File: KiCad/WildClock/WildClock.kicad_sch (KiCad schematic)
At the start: 33 parts, among them J1 UART, Q1 CA1, Q2 CA2, Q3 CA3, Q4 CA4, SW1 ButtonUp, SW2 ButtonDown, SW3 ButtonOK, U1 ESP32-C3-MINI-1, U3 74HC595, U4 TiltSensor

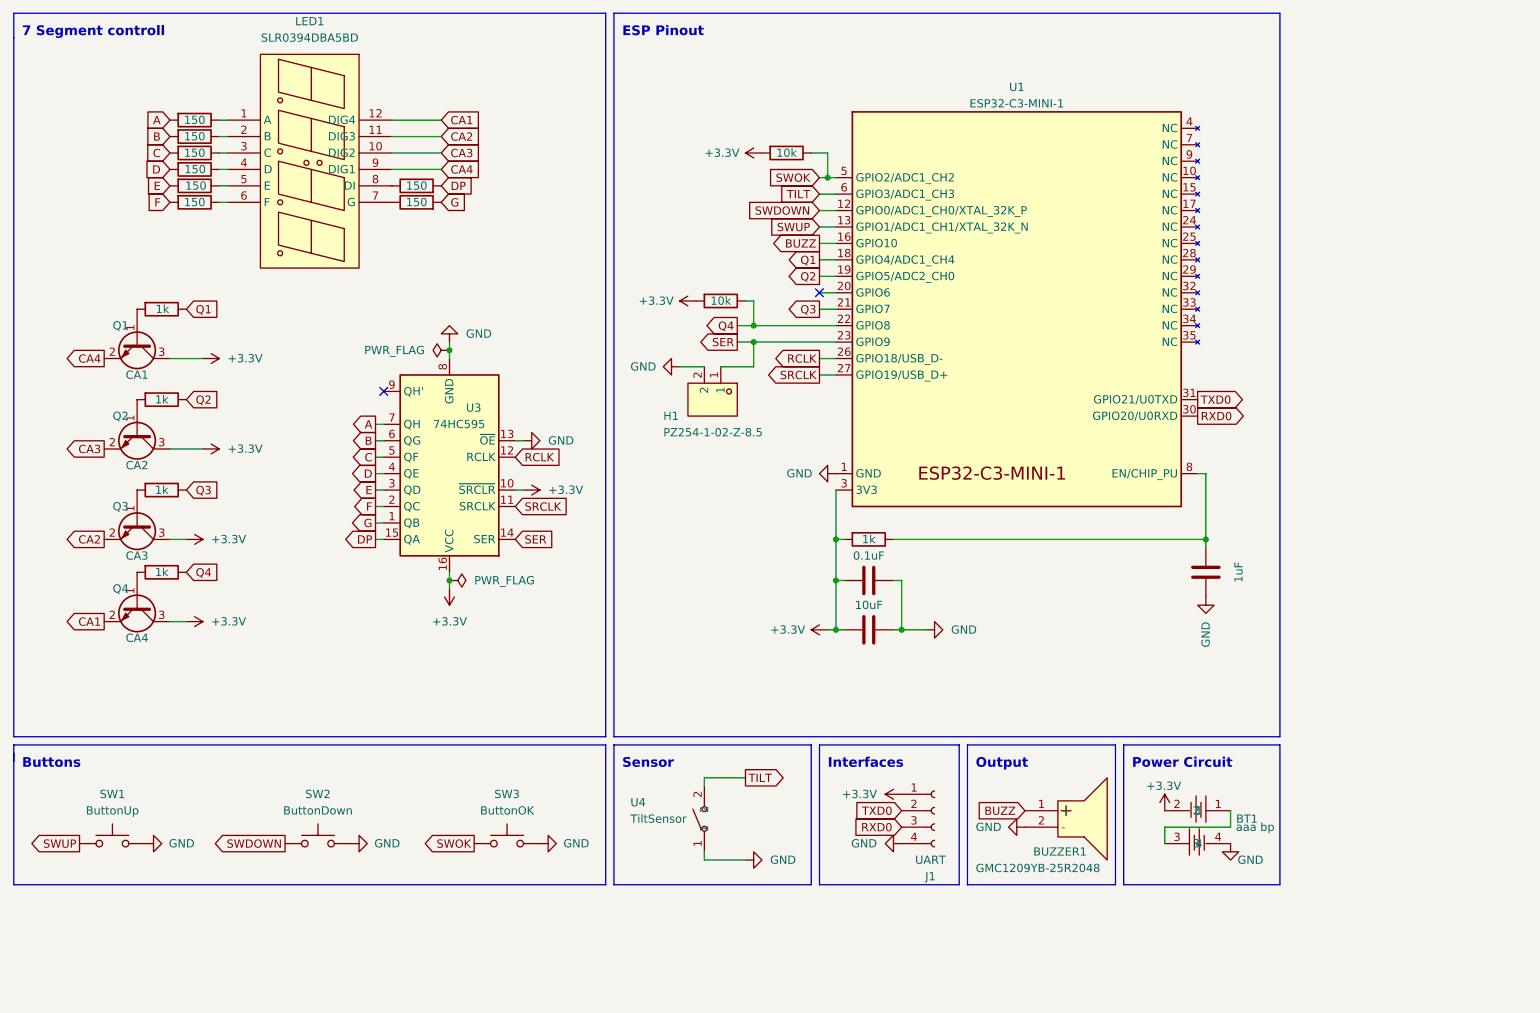
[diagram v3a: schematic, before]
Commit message: use lcsc footprints
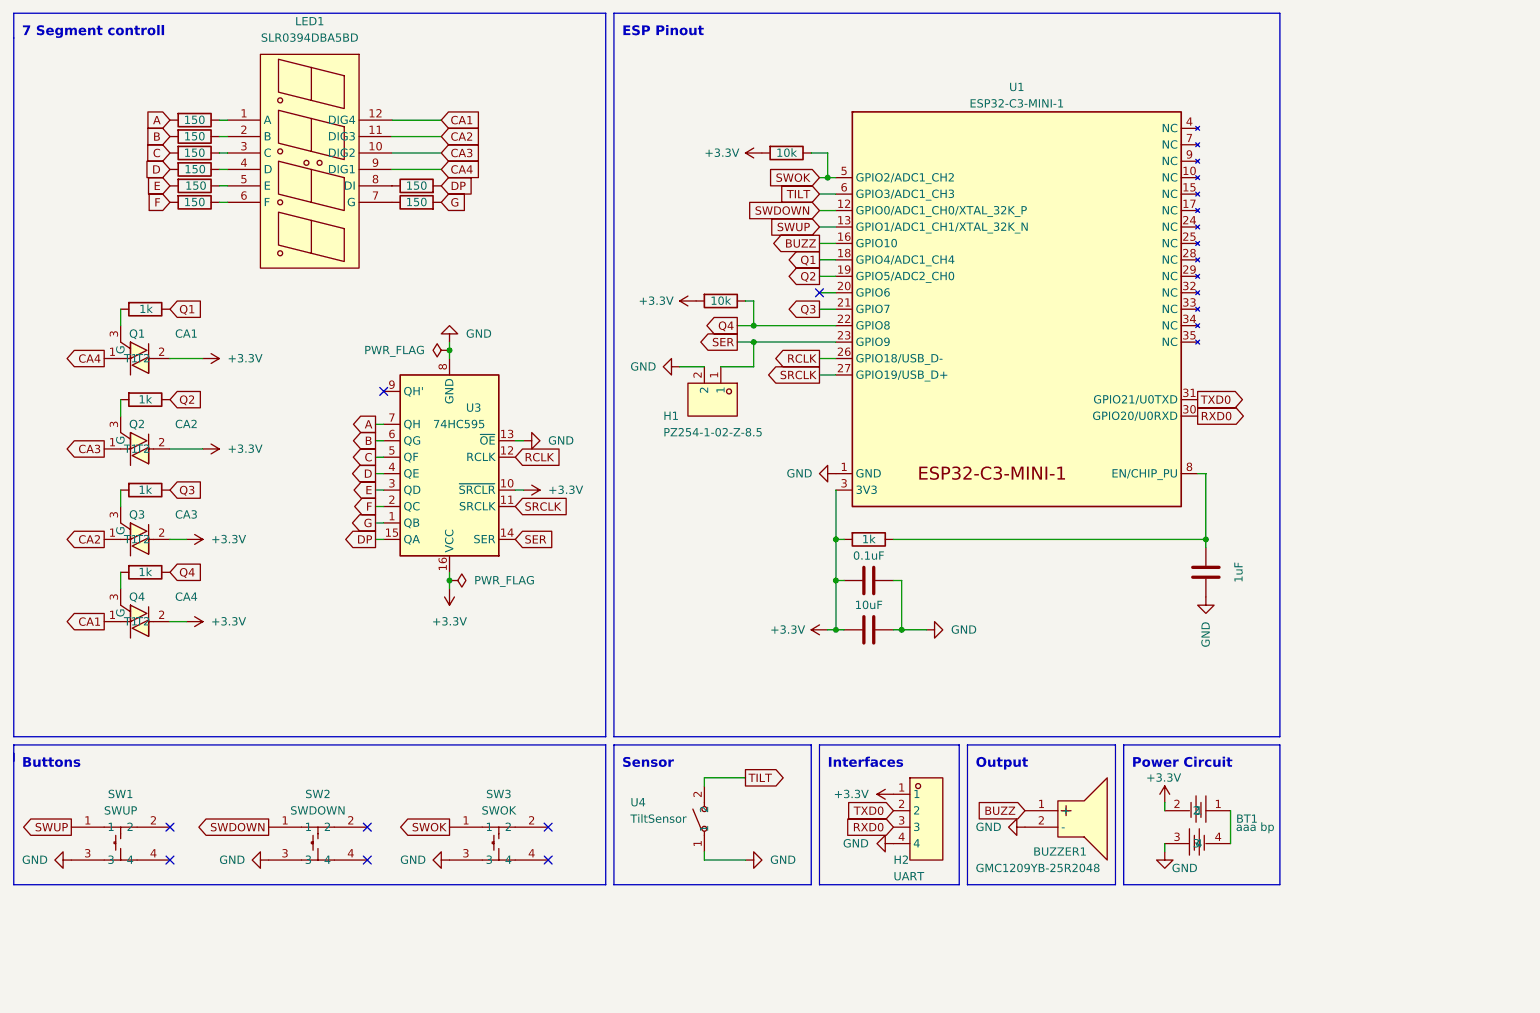
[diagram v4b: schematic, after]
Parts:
- removed J1: UART, Connector_PinHeader_1.00mm:PinHeader_1x04_P1.00mm_Vertical, symbol Connector:Conn_01x04_Female
- removed Q1: CA1, Package_TO_SOT_SMD:SOT-23, symbol Transistor_BJT:MMBT3904
- removed Q2: CA2, Package_TO_SOT_SMD:SOT-23, symbol Transistor_BJT:MMBT3904
- removed Q3: CA3, Package_TO_SOT_SMD:SOT-23, symbol Transistor_BJT:MMBT3904
- removed Q4: CA4, Package_TO_SOT_SMD:SOT-23, symbol Transistor_BJT:MMBT3904
- removed SW1: ButtonUp, Button_Switch_SMD:SW_Push_1P1T_NO_6x6mm_H9.5mm, symbol Switch:SW_Push
- removed SW2: ButtonDown, Button_Switch_SMD:SW_Push_1P1T_NO_6x6mm_H9.5mm, symbol Switch:SW_Push
- removed SW3: ButtonOK, Button_Switch_SMD:SW_Push_1P1T_NO_6x6mm_H9.5mm, symbol Switch:SW_Push
- added H2: UART, easyeda2kicad:HDR-TH_4P-P2.54-V-M, symbol easyeda2kicad:PZ254-1-04-Z-8.5
- added Q1: CA1, easyeda2kicad:SOT-23-3_L2.9-W1.3-P1.90-LS2.4-BR-CW, symbol easyeda2kicad:BT169-23
- added Q2: CA2, easyeda2kicad:SOT-23-3_L2.9-W1.3-P1.90-LS2.4-BR-CW, symbol easyeda2kicad:BT169-23
- added Q3: CA3, easyeda2kicad:SOT-23-3_L2.9-W1.3-P1.90-LS2.4-BR-CW, symbol easyeda2kicad:BT169-23
- added Q4: CA4, easyeda2kicad:SOT-23-3_L2.9-W1.3-P1.90-LS2.4-BR-CW, symbol easyeda2kicad:BT169-23
- added SW1: SWUP, easyeda2kicad:SW-TH_4P-L6.0-W6.0-P4.50-LS6.5, symbol easyeda2kicad:TS-1002-10526
- added SW2: SWDOWN, easyeda2kicad:SW-TH_4P-L6.0-W6.0-P4.50-LS6.5, symbol easyeda2kicad:TS-1002-10526
- added SW3: SWOK, easyeda2kicad:SW-TH_4P-L6.0-W6.0-P4.50-LS6.5, symbol easyeda2kicad:TS-1002-10526
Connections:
- net +3.3V: now also H2.1, Q1.2 (T2), Q2.2 (T2), Q3.2 (T2), Q4.2 (T2)
- net CA1: now also Q4.1 (T1)
- net CA2: now also Q3.1 (T1)
- net CA3: now also Q2.1 (T1)
- net CA4: now also Q1.1 (T1)
- net GND: now also BT1.3, H2.4, SW1.3, SW2.3, SW3.3; no longer BT1.4
- net RXD0: now also H2.3
- net SWDOWN: now also SW2.1
- net SWOK: now also SW3.1
- net SWUP: now also SW1.1
- net TXD0: now also H2.2
- net at R2.2: now also Q2.3 (G)
- net at R4.2: now also Q4.3 (G)
- net at R1.2: now also Q1.3 (G)
- net at BT1.1: now also BT1.4; no longer BT1.3
- net at R3.2: now also Q3.3 (G)
- no-connect marks 2 -> 8

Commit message: implemented maxis changes
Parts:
- removed Q1: CA1, easyeda2kicad:SOT-23-3_L2.9-W1.3-P1.90-LS2.4-BR-CW, symbol easyeda2kicad:BT169-23
- removed Q2: CA2, easyeda2kicad:SOT-23-3_L2.9-W1.3-P1.90-LS2.4-BR-CW, symbol easyeda2kicad:BT169-23
- removed Q3: CA3, easyeda2kicad:SOT-23-3_L2.9-W1.3-P1.90-LS2.4-BR-CW, symbol easyeda2kicad:BT169-23
- removed Q4: CA4, easyeda2kicad:SOT-23-3_L2.9-W1.3-P1.90-LS2.4-BR-CW, symbol easyeda2kicad:BT169-23
- added Q1, Q2, Q3, Q4: AO3401A, Package_TO_SOT_SMD:SOT-23, symbol Transistor_FET:AO3401A
- added Q5: AO3400A, Package_TO_SOT_SMD:SOT-23, symbol Transistor_FET:AO3400A
- added R5: 1k, Resistor_SMD:R_0805_2012Metric, symbol Device:R
- R2: value 1k -> 70
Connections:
- net +3.3V: now also R2.1, Q1.2 (S), Q2.2 (S), Q3.2 (S), Q4.2 (S)
- net BUZZ: now also Q5.1 (G); no longer BUZZER1.1 (+)
- net CA1: now also Q4.3 (D)
- net CA2: now also Q3.3 (D)
- net CA3: now also Q2.3 (D)
- net CA4: now also Q1.3 (D)
- net GND: now also Q5.2 (S); no longer BUZZER1.2 (-)
- net Q1: now also R1.2; no longer R1.1
- net Q2: now also R3.2; no longer R2.1
- net Q3: now also R4.2; no longer R3.1
- net Q4: now also R5.2; no longer R4.1
- net at R2.2: now also BUZZER1.1 (+)
- new net: Q2.1 (G), R3.1
- new net: Q1.1 (G), R1.1
- new net: Q4.1 (G), R5.1
- new net: Q3.1 (G), R4.1
- new net: BUZZER1.2 (-), Q5.3 (D)
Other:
- moved on the sheet: BT1, BUZZER1

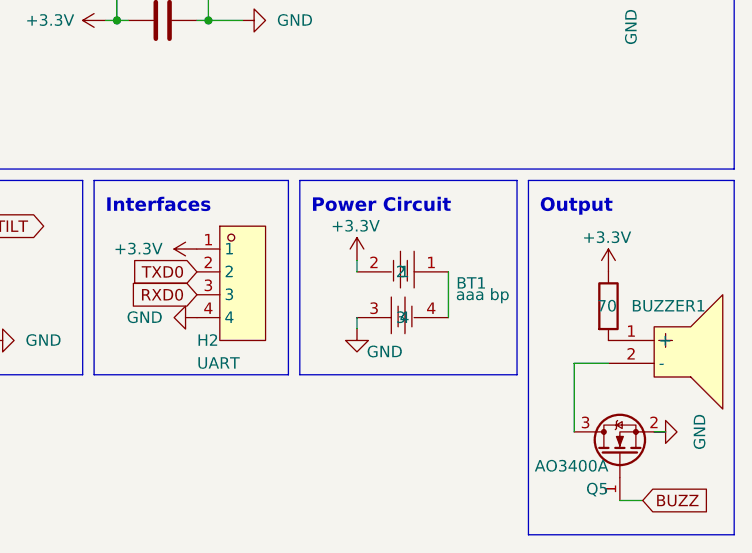
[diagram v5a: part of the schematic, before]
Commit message: fix batterie orientation
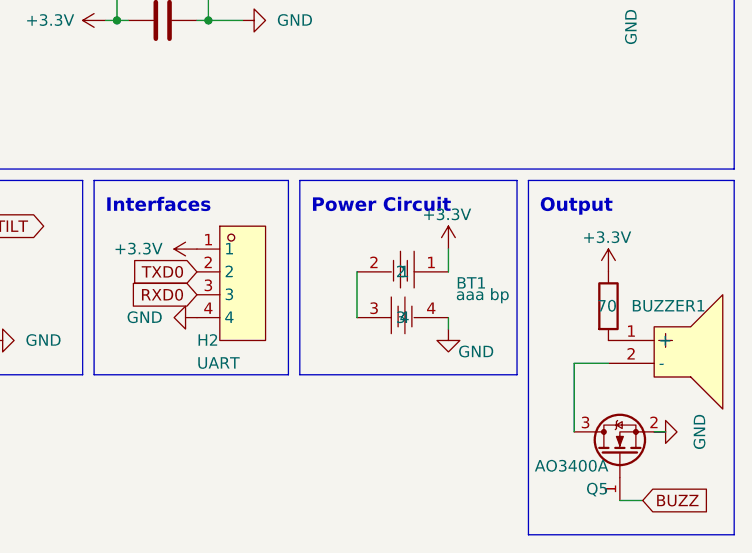
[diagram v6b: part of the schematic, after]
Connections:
- net +3.3V: now also BT1.1; no longer BT1.2
- net GND: now also BT1.4; no longer BT1.3
- new net: BT1.2, BT1.3
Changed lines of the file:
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@@
+    (stroke (width 0) (type default))
+  )
+  (wire (pts (xy 176.53 140.97) (xy 176.53 142.24))
     (stroke (width 0) (type default))
   )
@@
     (stroke (width 0) (type default))
   )
-  (wire (pts (xy 166.37 134.62) (xy 166.37 135.89))
+  (wire (pts (xy 176.53 133.35) (xy 176.53 135.89))
     (stroke (width 0) (type default))
   )
@@
     (stroke (width 0) (type default))
   )
-  (wire (pts (xy 176.53 135.89) (xy 176.53 140.97))
+  (wire (pts (xy 166.37 135.89) (xy 166.37 140.97))
     (stroke (width 0) (type default))
   )
@@
   )
   (wire (pts (xy 80.01 64.77) (xy 80.01 66.04))
-    (stroke (width 0) (type default))
-  )
-  (wire (pts (xy 166.37 140.97) (xy 166.37 142.24))
     (stroke (width 0) (type default))
   )
@@
     )
   )
-  (symbol (lib_id "power:+3.3V") (at 166.37 134.62 0) (unit 1)
-    (in_bom yes) (on_board yes) (dnp no)
-    (property "Reference" "#PWR024" (at 166.37 138.43 0)
-      (effects (font (size 1.27 1.27)) hide)
-    )
-    (property "Value" "+3.3V" (at 168.91 130.81 0)
+  (symbol (lib_id "power:+3.3V") (at 176.53 133.35 0) (unit 1)
+    (in_bom yes) (on_board yes) (dnp no)
+    (property "Reference" "#PWR024" (at 176.53 137.16 0)
+      (effects (font (size 1.27 1.27)) hide)
+    )
+    (property "Value" "+3.3V" (at 179.07 129.54 0)
       (effects (font (size 1.27 1.27)) (justify right))
     )
-    (property "Footprint" "" (at 166.37 134.62 0)
-      (effects (font (size 1.27 1.27)) hide)
-    )
-    (property "Datasheet" "" (at 166.37 134.62 0)
+    (property "Footprint" "" (at 176.53 133.35 0)
+      (effects (font (size 1.27 1.27)) hide)
+    )
+    (property "Datasheet" "" (at 176.53 133.35 0)
       (effects (font (size 1.27 1.27)) hide)
     )
@@
     )
   )
-  (symbol (lib_id "power:GND") (at 166.37 142.24 0) (unit 1)
-    (in_bom yes) (on_board yes) (dnp no)
-    (property "Reference" "#PWR025" (at 166.37 148.59 0)
-      (effects (font (size 1.27 1.27)) hide)
-    )
-    (property "Value" "GND" (at 171.45 144.78 0)
+  (symbol (lib_id "power:GND") (at 176.53 142.24 0) (unit 1)
+    (in_bom yes) (on_board yes) (dnp no)
+    (property "Reference" "#PWR025" (at 176.53 148.59 0)
+      (effects (font (size 1.27 1.27)) hide)
+    )
+    (property "Value" "GND" (at 181.61 144.78 0)
       (effects (font (size 1.27 1.27)) (justify right))
     )
-    (property "Footprint" "" (at 166.37 142.24 0)
-      (effects (font (size 1.27 1.27)) hide)
-    )
-    (property "Datasheet" "" (at 166.37 142.24 0)
-      (effects (font (size 1.27 1.27)) hide)
-    )
+    (property "Footprint" "" (at 176.53 142.24 0)
+      (effects (font (size 1.27 1.27)) hide)
+    )
+    (property "Datasheet" "" (at 176.53 142.24 0)
+      (effects (font (size 1.27 1.27)) hide)
+    )
